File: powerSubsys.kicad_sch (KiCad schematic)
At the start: 4 parts, among them J1 Conn_02x16_Odd_Even, J2 JST_PH_2mm, U1 INA219AxD

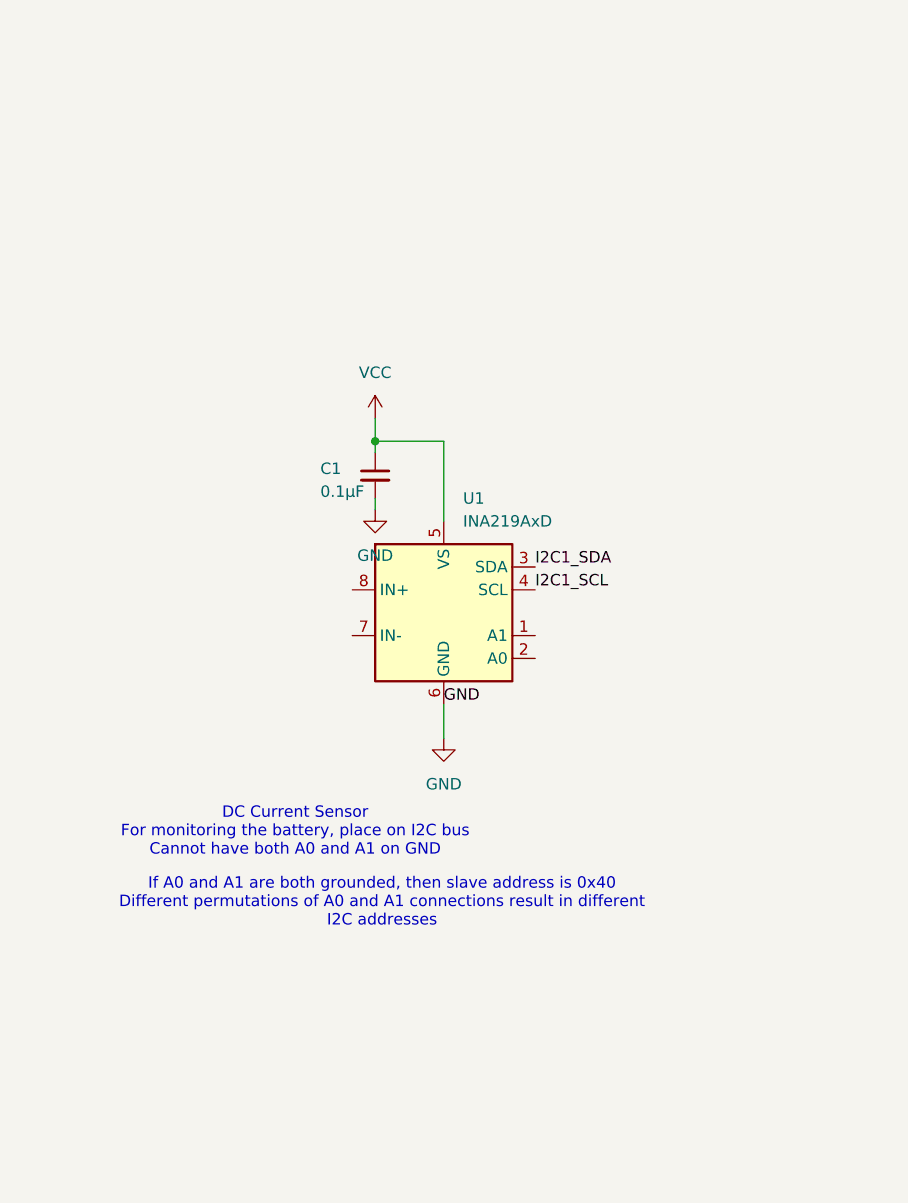
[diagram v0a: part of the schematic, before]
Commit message: Add files via upload
- Progressed INA219 current sensor
- Set new I2C address config to not conflict with sensor module
- Neatened up design
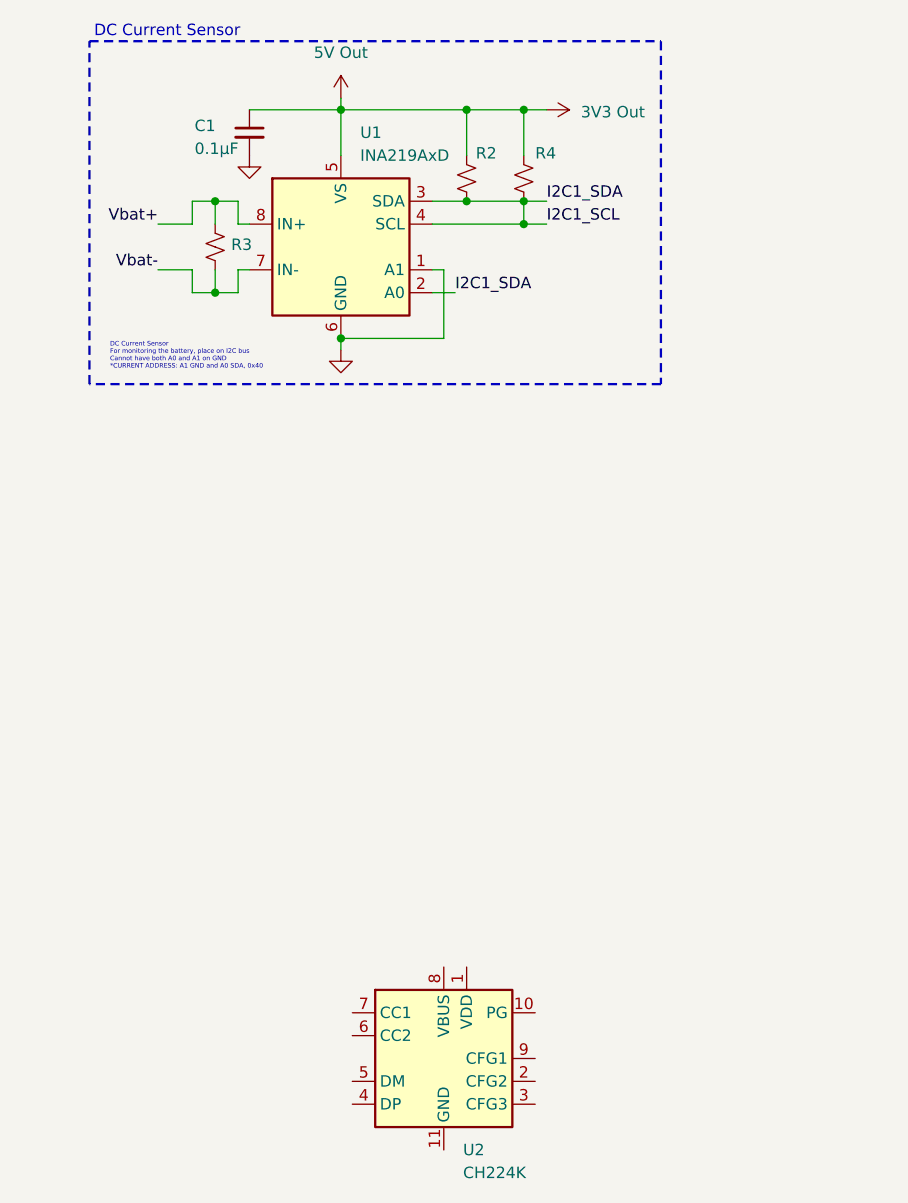
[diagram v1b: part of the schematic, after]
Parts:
- added R2, R3, R4: R_Small_US, symbol Device:R_Small_US
- added U2: CH224K, Package_SO:SSOP-10-1EP_3.9x4.9mm_P1mm_EP2.1x3.3mm, symbol Interface_USB:CH224K
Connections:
- net 5V Out is gone; now on net 3V3 Out: J1.20 (Pin_20)
- net I2C1_SDA is gone; now on net I2C1_SCL: J1.17 (Pin_17), U1.3 (SDA)
- net VCC is gone; now on net 3V3 Out: C1.1, U1.5 (VS)
- net 3V3 Out: now also R2.1, R4.1
- net GND: now also U1.1 (A1)
- net I2C1_SCL: now also U1.2 (A0), R2.2, R4.2
- net Vbat+: now also U1.8 (IN+), R3.1
- net Vbat-: now also U1.7 (IN-), R3.2
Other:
- note added: "DC Current Sensor"
- note added: "DC Current Sensor For monitoring the battery, place on I2C bus Cannot have both A0 and A1 on GND *CURRENT ADDRESS: A1 GND and A0 SDA, 0x40"
- note removed: "DC Current Sensor For monitoring the battery, place on I2C bus Cannot have both A0 and A1 on GND"
- note removed: "If A0 and A1 are both grounded, then slave address is 0x40 Different permutations of A0 and A1 connections result in different I2C addresses"
- moved on the sheet: C1, U1

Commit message: Added the charging controller
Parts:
- added U3: BQ24075RGT, Package_DFN_QFN:VQFN-16-1EP_3x3mm_P0.5mm_EP1.6x1.6mm, symbol Battery_Management:BQ24075RGT
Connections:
- net GND: now also U3.17 (VSS), U3.8 (VSS)
- new net: U3.10 (OUT), U3.11 (OUT)
- new net: U3.2 (BAT), U3.3 (BAT)
- new net +9V: U3.13 (IN)

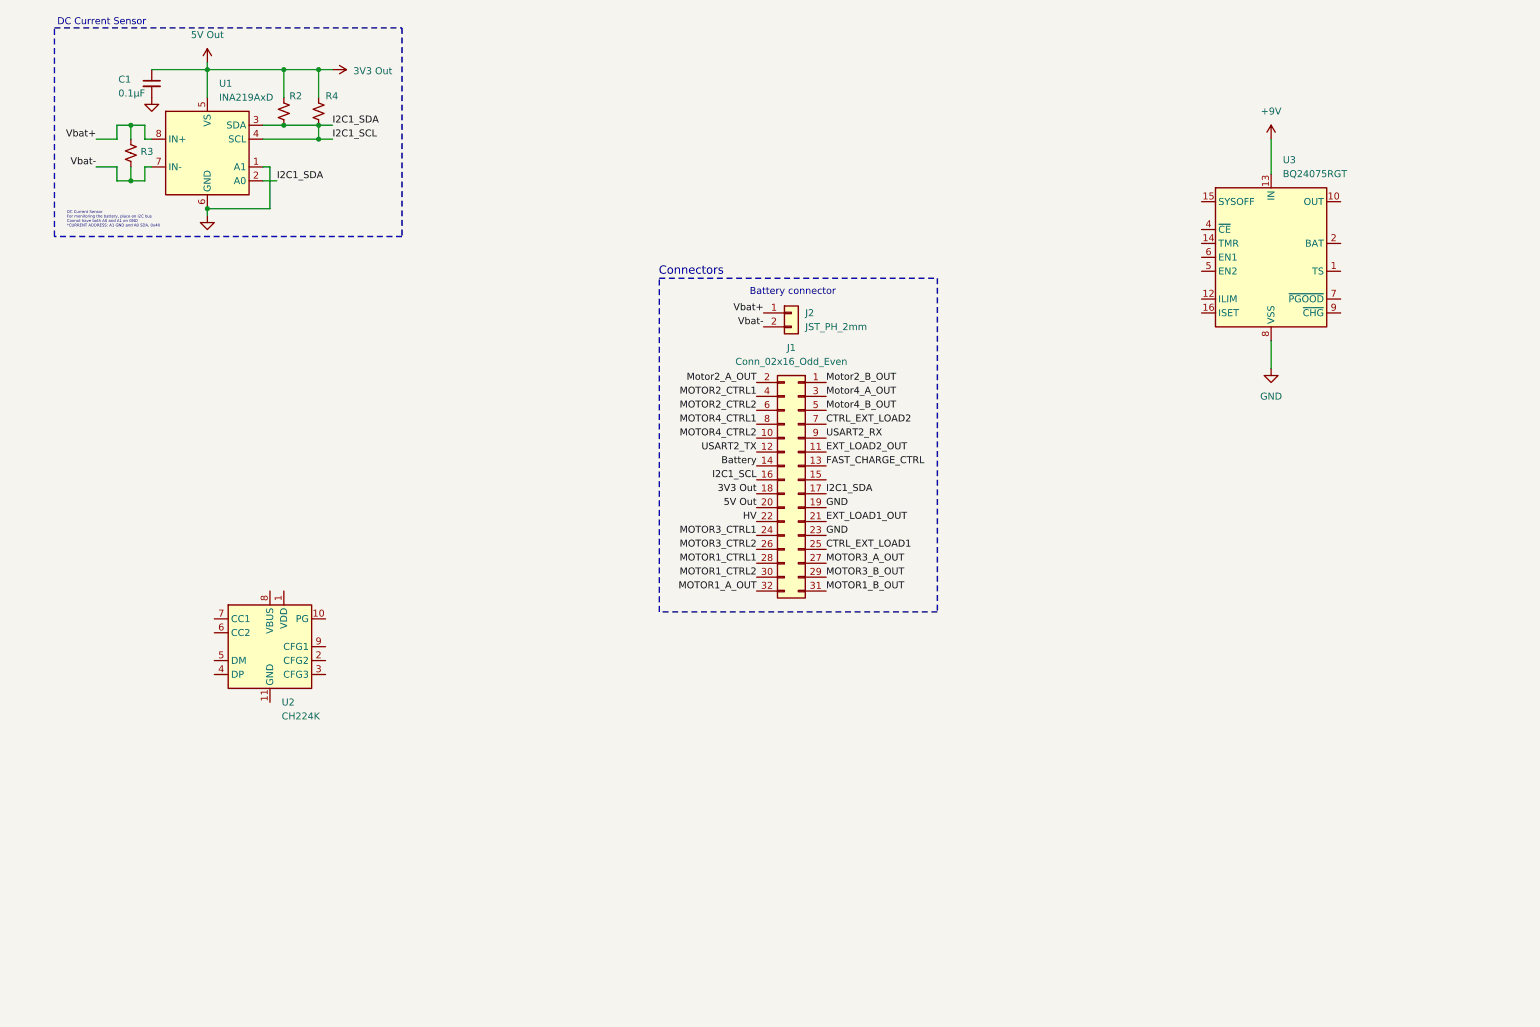
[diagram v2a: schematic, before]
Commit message: Added: Charge Controller and Load Switches
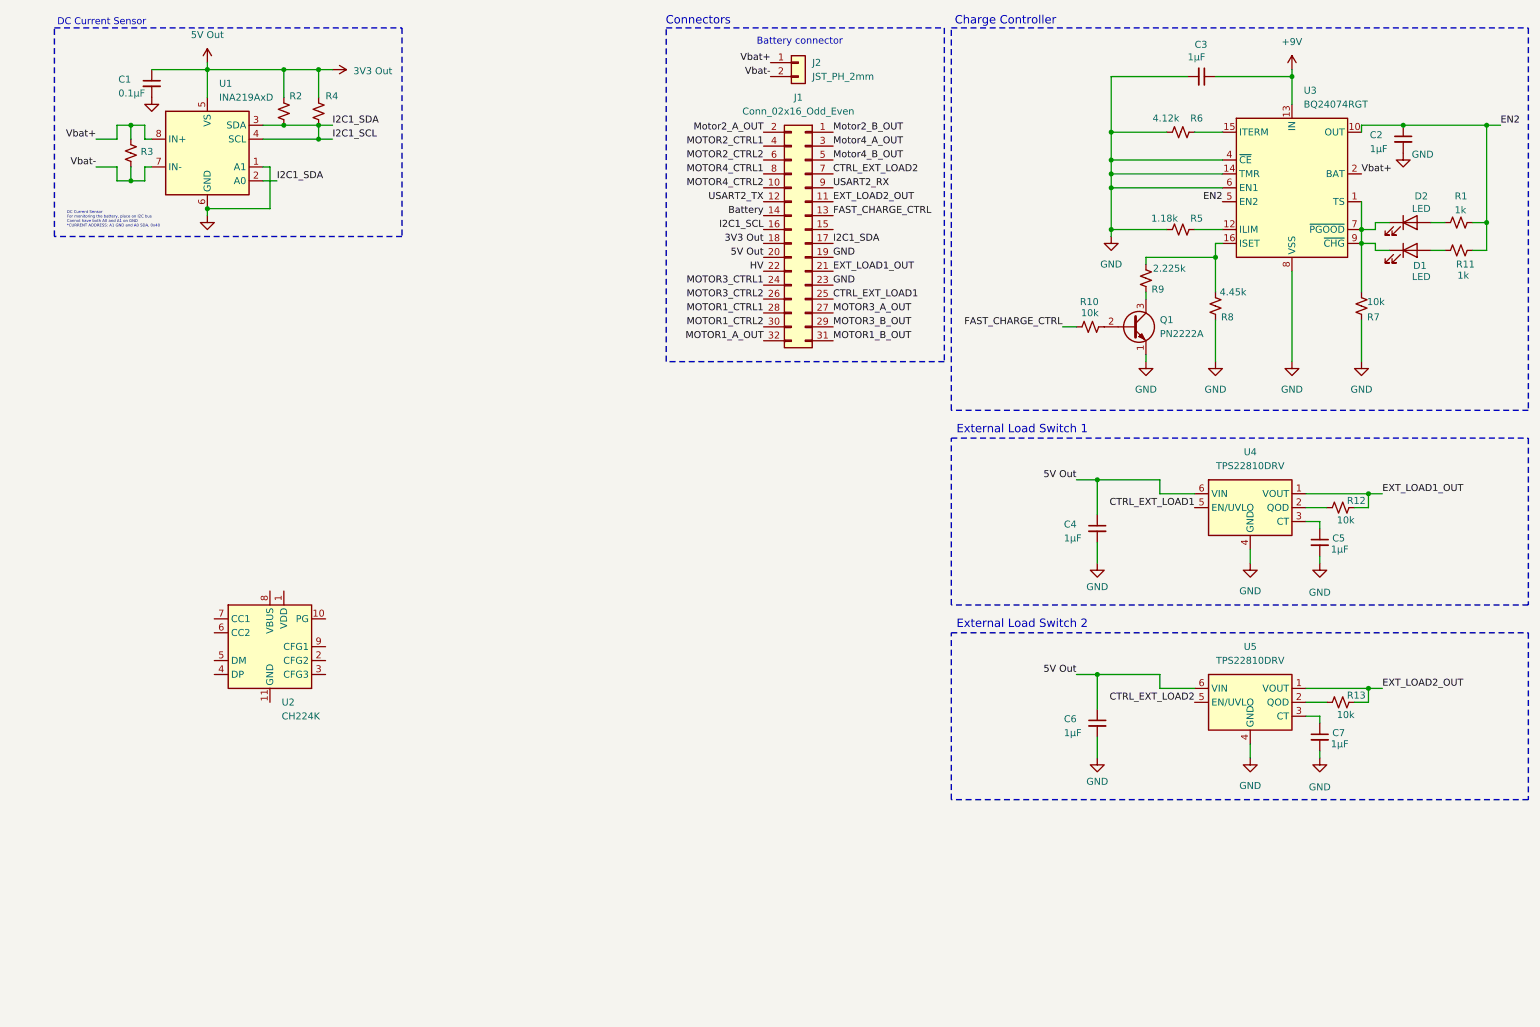
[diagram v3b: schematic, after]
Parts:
- removed U3: BQ24075RGT, Package_DFN_QFN:VQFN-16-1EP_3x3mm_P0.5mm_EP1.6x1.6mm, symbol Battery_Management:BQ24075RGT
- added C2, C3, C4, C5, C6, C7: 1μF, symbol Device:C_Small
- added D1, D2: LED, symbol Device:LED
- added Q1: PN2222A, Package_TO_SOT_THT:TO-92_Inline, symbol Transistor_BJT:PN2222A
- added R10, R12, R13, R7: 10k, symbol Device:R_Small_US
- added R11: 1k, symbol Device:R_Small_US
- added R5: 1.18k, symbol Device:R_Small_US
- added R6: 4.12k, symbol Device:R_Small_US
- added R8: 4.45k, symbol Device:R_Small_US
- added R9: 2.225k, symbol Device:R_Small_US
- added U3: BQ24074RGT, Package_DFN_QFN:VQFN-16-1EP_3x3mm_P0.5mm_EP1.6x1.6mm, symbol Battery_Management:BQ24074RGT
- added U4, U5: TPS22810DRV, Package_SON:WSON-6-1EP_2x2mm_P0.65mm_EP1x1.6mm, symbol Power_Management:TPS22810DRV
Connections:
- net +9V: now also C3.1, U3.13 (IN)
- net 3V3 Out: now also C4.1, C6.1, U4.6 (VIN), U5.6 (VIN)
- net CTRL_EXT_LOAD1: now also U4.5 (EN/UVLO)
- net CTRL_EXT_LOAD2: now also U5.5 (EN/UVLO)
- net EXT_LOAD1_OUT: now also R12.2, U4.1 (VOUT)
- net EXT_LOAD2_OUT: now also R13.2, U5.1 (VOUT)
- net FAST_CHARGE_CTRL: now also R10.1
- net GND: now also C2.2, C3.2, C4.2, C5.2, C6.2, C7.2, Q1.1 (E), R5.1, R6.1, R7.2, R8.2, U3.14 (TMR), U3.17 (VSS), U3.4 (~{CE}), U3.6 (EN1), U3.8 (VSS), U4.4 (GND), U4.7 (GND), U5.4 (GND), U5.7 (GND)
- net Vbat+: now also U3.2 (BAT), U3.3 (BAT)
- new net: R13.1, U5.2 (QOD)
- new net: C7.1, U5.3 (CT)
- new net: R8.1, R9.1, U3.16 (ISET)
- new net: Q1.3 (C), R9.2
- new net: Q1.2 (B), R10.2
- new net: D1.1 (K), D2.1 (K), R7.1, U3.1 (TS), U3.7 (~{PGOOD}), U3.9 (~{CHG})
- new net: D2.2 (A), R2.2
- new net: C5.1, U4.3 (CT)
- new net: R12.1, U4.2 (QOD)
- new net: R5.2, U3.12 (ILIM)
- new net: D1.2 (A), R11.2
- new net: R6.2, U3.15 (ITERM)
- new net EN2: C2.1, R11.1, R2.1, U3.10 (OUT), U3.11 (OUT), U3.5 (EN2)
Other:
- note added: "Charge Controller"
- note added: "External Load Switch 1"
- note added: "External Load Switch 2"
- moved on the sheet: J1, J2, R1

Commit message: Cleaning and addition
Cleaned up schematic
Added H-bridge IC
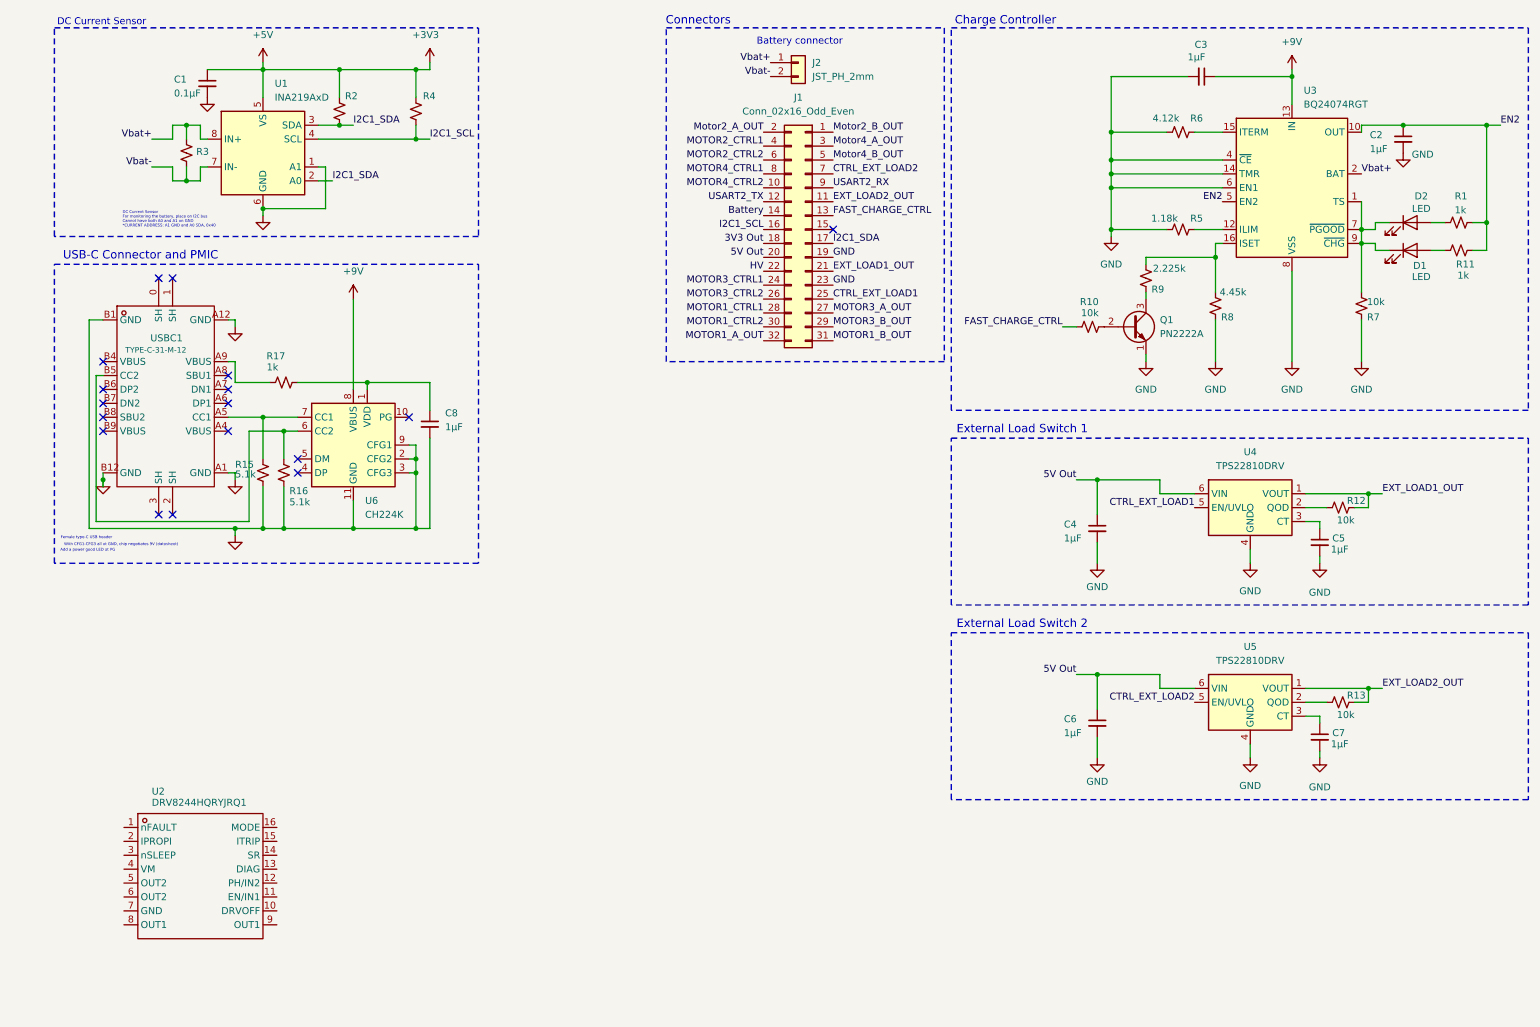
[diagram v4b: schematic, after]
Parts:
- removed U2: CH224K, Package_SO:SSOP-10-1EP_3.9x4.9mm_P1mm_EP2.1x3.3mm, symbol Interface_USB:CH224K
- added C8: 1μF, symbol Device:C_Small
- added R15, R16: 5.1k, symbol Device:R_Small_US
- added R17: 1k, symbol Device:R_Small_US
- added R2: R_Small_US, symbol Device:R_Small_US
- added U2: DRV8244HQRYJRQ1, VQFN-16_L6.0-W3.0-P0.50-TL, symbol DRV8244HQRYJRQ11_DRV8244HQRYJRQ1-altium-import:root_0_DRV8244HQRYJRQ1_
- added U6: CH224K, Package_SO:SSOP-10-1EP_3.9x4.9mm_P1mm_EP2.1x3.3mm, symbol Interface_USB:CH224K
- added USBC1: TYPE-C-31-M-12, USB-C_SMD-TYPE-C-31-M-12, symbol usb_c-altium-import:root_0_TYPE-C-31-M-12_
- R1: renamed from R2; value R_Small_US -> 1k
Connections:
- net +9V: now also U6.8 (VBUS)
- net 3V3 Out: no longer C1.1, C4.1, C6.1, J1.20 (Pin_20), R1.1, R4.1, U1.5 (VS), U4.6 (VIN), U5.6 (VIN)
- net GND: now also C8.2, R15.2, R16.2, U6.11 (GND), U6.2 (CFG2), U6.3 (CFG3), U6.9 (CFG1), USBC1.A1 (GND), USBC1.A12 (GND), USBC1.B1 (GND), USBC1.B12 (GND)
- net I2C1_SCL: no longer J1.17 (Pin_17), R1.2, U1.2 (A0), U1.3 (SDA)
- new net: R16.1, U6.6 (CC2), USBC1.B5 (CC2)
- new net: R17.1, USBC1.A9 (VBUS)
- new net: C8.1, R17.2, U6.1 (VDD)
- new net: R15.1, U6.7 (CC1), USBC1.A5 (CC1)
- new net +3V3: C1.1, R2.1, R4.1, U1.5 (VS)
- new net 5V Out: C4.1, C6.1, J1.20 (Pin_20), U4.6 (VIN), U5.6 (VIN)
- new net I2C1_SDA: J1.17 (Pin_17), R2.2, U1.2 (A0), U1.3 (SDA)
- no-connect marks 0 -> 17
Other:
- note added: "Add a power good LED at PG"
- note added: "Female type-C USB header"
- note added: "USB-C Connector and PMIC"
- note added: "With CFG1-CFG3 all at GND, chip negotiates 9V (datasheet)"
- moved on the sheet: C1, R3, R4, U1
